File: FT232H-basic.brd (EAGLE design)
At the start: 45.7 x 20.3 mm, 29 parts, among them IC1 FT232H

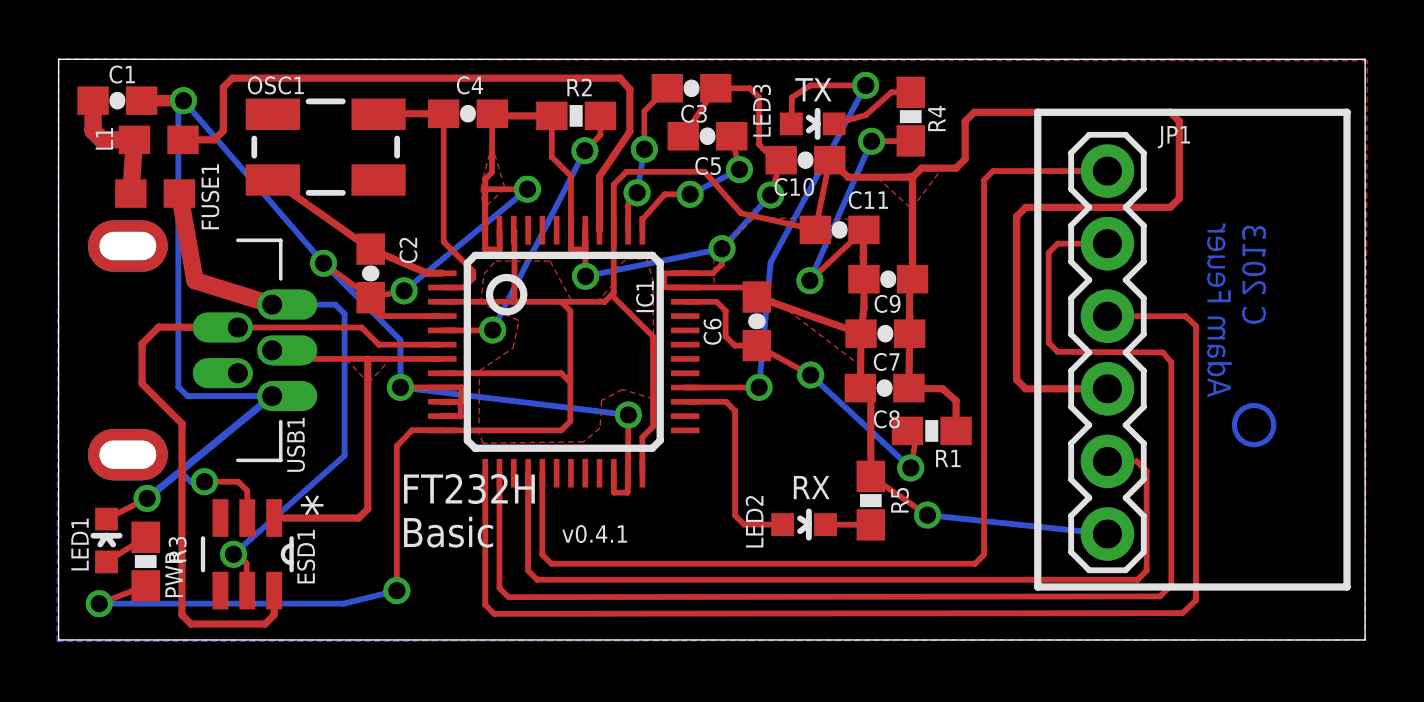
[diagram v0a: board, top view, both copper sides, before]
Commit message: replaced decoupling capacitors close to chip; rerouted board
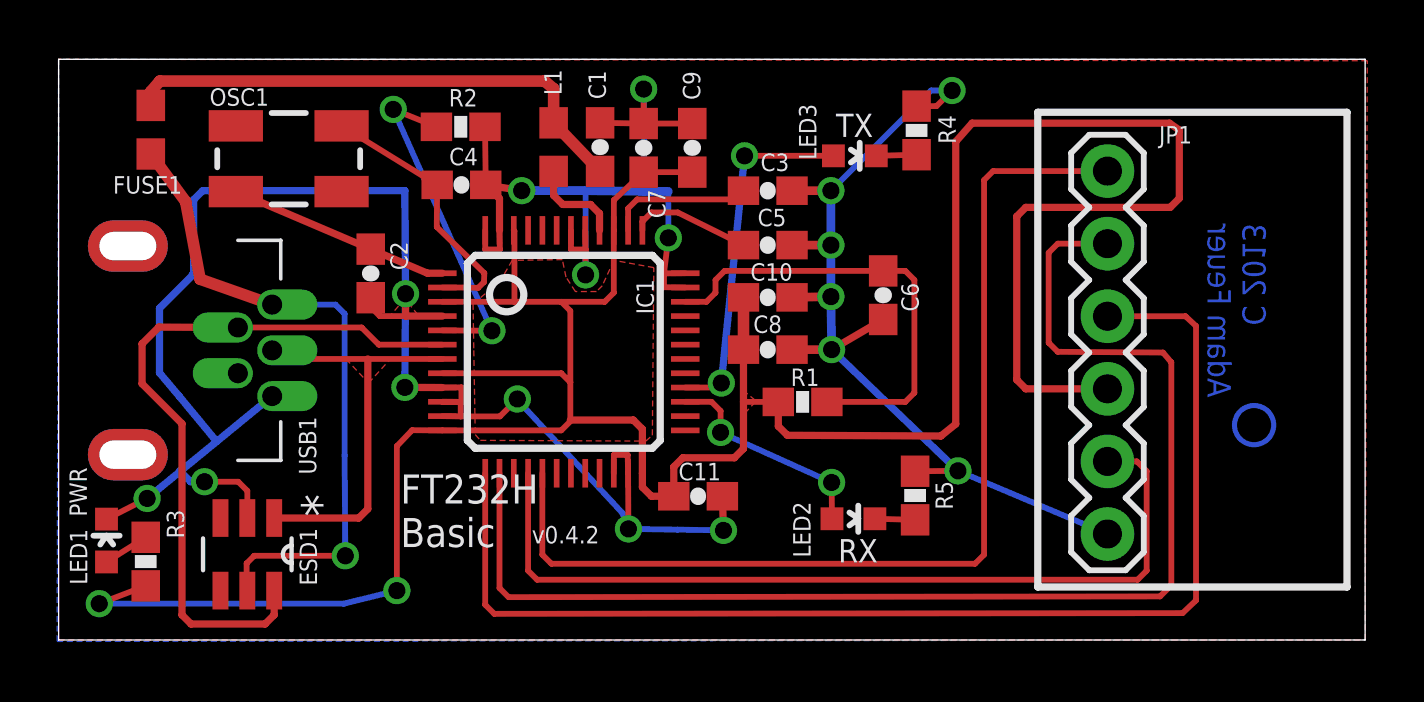
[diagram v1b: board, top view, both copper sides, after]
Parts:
- moved C1 17.0 mm to (25.3, 21.1), turned to 90 degrees
- moved L1 13.8 mm to (23.7, 21.1), turned to 270 degrees
- moved C7 10.7 mm to (26.8, 21.0), turned to 90 degrees
- moved C11 10.6 mm to (28.7, 8.84)
- moved C9 8.26 mm to (28.5, 21.0), turned to 90 degrees
- moved C10 4.98 mm to (31.2, 15.8), turned to 0 degrees
- moved R1 4.63 mm to (32.4, 12.1), turned to 180 degrees
- moved C6 4.51 mm to (35.2, 15.9), turned to 270 degrees
- moved C3 4.47 mm to (31.2, 19.5)
- moved C5 4.35 mm to (31.2, 17.6), turned to 0 degrees
- moved C8 4.31 mm to (31.2, 14.0), turned to 0 degrees
- moved R2 4.06 mm to (20.4, 21.8), turned to 180 degrees
- moved C4 2.50 mm to (20.4, 19.7)
- moved FUSE1 2.24 mm to (9.58, 21.7), turned to 90 degrees
- moved LED3 1.85 mm to (34.2, 20.8)
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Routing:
- net VREGIN: track 22.9 -> 3.30 mm
- net N$6: track 4.52 -> 18.4 mm
- net GND: track 138.7 -> 125.7 mm, vias 14 -> 17
- net TXLED: track 17.6 -> 12.4 mm
- net N$3: track 12.0 -> 16.0 mm, vias 2 -> 0
- net VUSB: track 20.3 -> 23.2 mm
- net N$10: track 3.02 -> 1.41 mm
- net N$4: track 10.3 -> 11.8 mm
- net N$1: track 5.58 -> 4.25 mm, vias 2 -> 0
- net POWER: track 105.4 -> 106.6 mm
- net OSC1: track 6.87 -> 7.81 mm
- net N$2: track 5.43 -> 5.06 mm, vias 2 -> 0
- net RXLED: track 7.33 -> 7.65 mm, vias 0 -> 2
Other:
- board text added: "v0.4.2"
- board text removed: "v0.4.1"

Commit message: moved OSC1 traces so they are not serpentine
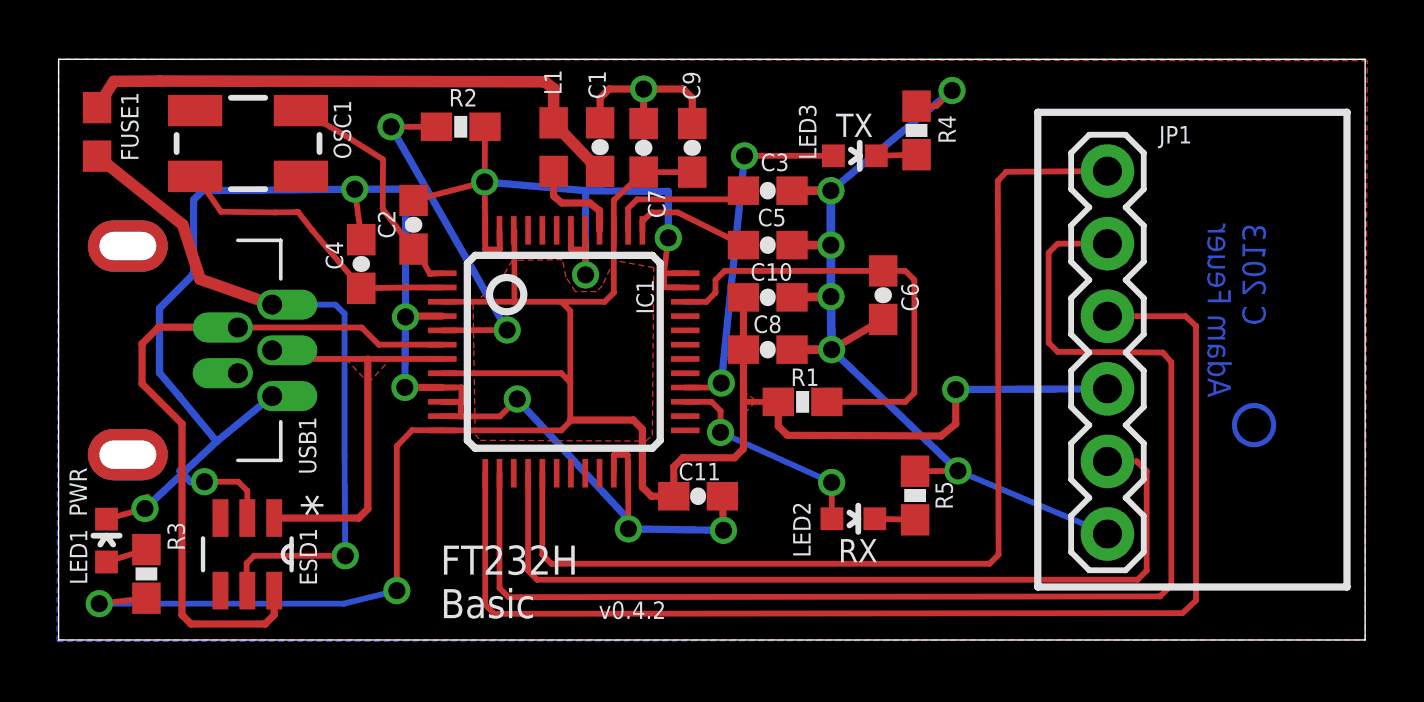
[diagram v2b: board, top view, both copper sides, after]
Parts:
- removed FRAME1: FRAME-LETTER, SparkFun-Aesthetics:CREATIVE_COMMONS
- moved U$1 19.9 mm to (38.1, 17.1)
- moved CC-BY-SA-LOGO 11.8 mm to (41.5, 4.37)
- moved C4 4.47 mm to (16.9, 17.0), turned to 90 degrees
- moved C2 2.27 mm to (18.8, 18.3), turned to 90 degrees
- moved FUSE1 1.88 mm to (7.70, 21.6)
- moved OSC1 1.52 mm to (13.0, 21.2), turned to 180 degrees
- moved R3 0.43 mm to (9.42, 6.12)
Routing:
- net POWER: track 106.6 -> 77.6 mm, vias 2 -> 3
- net GND: track 125.7 -> 128.5 mm, vias 17 -> 18
- net N$6: track 18.4 -> 20.1 mm
- net VUSB: track 23.2 -> 24.2 mm
- net N$7: track 9.58 -> 10.5 mm
- net OSC1: track 7.81 -> 8.34 mm
- removed copper zone on layer 1, net GND
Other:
- board text added: "3.3V"
- board text removed: "5V"

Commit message: moved VUSB trace so it doesn't cross under USB DP and DM - so there is only ground plane under the high speed traces
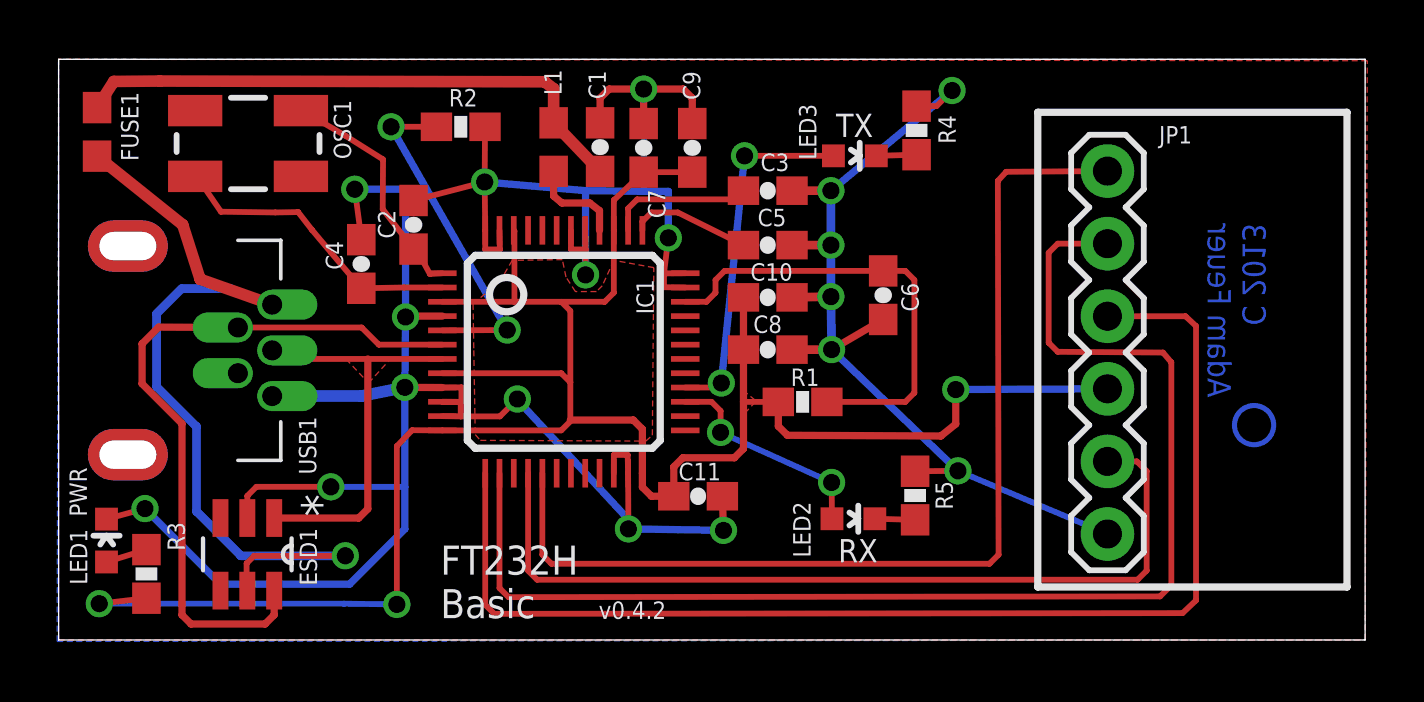
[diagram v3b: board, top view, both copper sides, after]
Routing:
- net VUSB: track 24.2 -> 30.9 mm
- net GND: track 128.5 -> 130.1 mm
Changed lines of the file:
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@@
 <contactref element="JP1" pad="6"/>
 <contactref element="C1" pad="2"/>
-<wire x1="9.4606" y1="8.802" x2="9.3726" y2="8.4074" width="0.254" layer="1"/>
 <via x="9.3726" y="8.4074" extent="1-16" drill="0.6"/>
-<wire x1="9.3726" y1="8.4074" x2="11.88134375" y2="10.75440625" width="0.254" layer="16"/>
-<wire x1="11.88134375" y1="10.75440625" x2="13.8238" y2="12.3446" width="0.254" layer="16"/>
-<wire x1="12.954" y1="8.0772" x2="12.954" y2="9.0297" width="0.2032" layer="1"/>
-<wire x1="12.954" y1="9.0297" x2="12.6365" y2="9.3472" width="0.2032" layer="1"/>
-<wire x1="12.6365" y1="9.3472" x2="11.4554" y2="9.3472" width="0.2032" layer="1"/>
-<via x="11.4554" y="9.3472" extent="1-16" drill="0.6"/>
-<wire x1="11.4554" y1="9.3472" x2="10.9727625" y2="9.3472" width="0.254" layer="16"/>
-<wire x1="10.9727625" y1="9.3472" x2="10.587325" y2="9.7326375" width="0.254" layer="16"/>
 <wire x1="24.2784" y1="17.4752" x2="24.2784" y2="18.1438" width="0.2032" layer="1"/>
 <wire x1="19.7784" y1="11.6438" x2="20.4216" y2="11.6332" width="0.2032" layer="1"/>
@@
 <wire x1="24.7904" y1="19.5326" x2="21.2598" y2="19.8374" width="0.254" layer="16"/>
 <wire x1="18.4912" y1="19.5834" x2="16.7132" y2="19.5834" width="0.254" layer="16"/>
-<wire x1="16.7132" y1="19.5834" x2="11.3919" y2="19.5326" width="0.254" layer="16"/>
-<wire x1="11.3919" y1="19.5326" x2="11.0744" y2="19.2151" width="0.254" layer="16"/>
-<wire x1="11.0744" y1="19.2151" x2="11.0744" y2="16.5862" width="0.254" layer="16"/>
-<wire x1="11.0744" y1="16.5862" x2="11.049" y2="16.5862" width="0.3048" layer="16"/>
-<wire x1="11.049" y1="16.5862" x2="9.8806" y2="15.4178" width="0.254" layer="16"/>
-<wire x1="9.8806" y1="15.4178" x2="9.8806" y2="13.1572" width="0.254" layer="16"/>
-<wire x1="9.8806" y1="13.1572" x2="10.5664" y2="12.3444" width="0.254" layer="16"/>
 <wire x1="32.0158" y1="17.6276" x2="33.3756" y2="17.6276" width="0.3048" layer="1"/>
 <via x="33.3756" y="17.6276" extent="1-16" drill="0.6"/>
@@
 <wire x1="37.0704" y1="22.4908" x2="37.6174" y2="23.0378" width="0.2032" layer="1"/>
 <via x="37.6174" y="23.0378" extent="1-16" drill="0.6"/>
-<wire x1="10.5664" y1="12.3444" x2="11.88134375" y2="10.75440625" width="0.254" layer="16"/>
 <wire x1="33.3756" y1="19.5326" x2="37.6174" y2="23.0378" width="0.254" layer="16"/>
 <wire x1="21.2716" y1="21.7678" x2="21.2598" y2="19.8374" width="0.2032" layer="1"/>
@@
 <wire x1="28.5242" y1="22.7711" x2="28.2067" y2="23.0886" width="0.254" layer="1"/>
 <wire x1="28.2067" y1="23.0886" x2="26.8224" y2="23.0886" width="0.254" layer="1"/>
+<wire x1="9.3726" y1="8.4074" x2="12.0142" y2="5.7658" width="0.254" layer="16"/>
+<wire x1="12.0142" y1="5.7658" x2="16.5354" y2="5.7658" width="0.254" layer="16"/>
+<wire x1="16.5354" y1="5.7658" x2="18.4658" y2="7.6962" width="0.254" layer="16"/>
+<wire x1="18.4658" y1="7.6962" x2="18.4658" y2="9.1694" width="0.254" layer="16"/>
+<wire x1="18.4658" y1="9.1694" x2="18.4658" y2="12.6492" width="0.254" layer="16"/>
+<wire x1="12.954" y1="8.0772" x2="12.954" y2="8.8519" width="0.2032" layer="1"/>
+<wire x1="12.954" y1="8.8519" x2="13.2715" y2="9.1694" width="0.2032" layer="1"/>
+<wire x1="13.2715" y1="9.1694" x2="15.875" y2="9.1694" width="0.2032" layer="1"/>
+<via x="15.875" y="9.1694" extent="1-16" drill="0.6"/>
+<wire x1="15.875" y1="9.1694" x2="18.4658" y2="9.1694" width="0.2032" layer="16"/>
+<wire x1="13.8238" y1="12.3446" x2="16.942" y2="12.3446" width="0.4064" layer="16"/>
+<wire x1="16.942" y1="12.3446" x2="18.4658" y2="12.6492" width="0.4064" layer="16"/>
 </signal>
 <signal name="OSC1">
@@
 <wire x1="12.954" y1="5.5372" x2="12.9286" y2="5.5626" width="0.254" layer="1"/>
 <via x="16.383" y="6.7564" extent="1-16" drill="0.6"/>
-<wire x1="16.3576" y1="15.2271" x2="16.0401" y2="15.5446" width="0.2032" layer="16"/>
-<wire x1="16.0401" y1="15.5446" x2="13.8238" y2="15.5446" width="0.2032" layer="16"/>
-<wire x1="16.3576" y1="15.2271" x2="16.3576" y2="10.2616" width="0.2032" layer="16"/>
-<wire x1="16.3576" y1="10.2616" x2="16.383" y2="6.7564" width="0.2032" layer="16"/>
 <wire x1="12.9286" y1="5.5626" x2="12.9286" y2="6.4897" width="0.2032" layer="1"/>
 <wire x1="12.9286" y1="6.4897" x2="13.1953" y2="6.7564" width="0.2032" layer="1"/>
@@
 <wire x1="11.303" y1="16.4338" x2="10.6934" y2="18.3388" width="0.4064" layer="1"/>
 <wire x1="10.6934" y1="18.3388" x2="7.6962" y2="20.74" width="0.4064" layer="1"/>
+<wire x1="13.8238" y1="15.5446" x2="12.3698" y2="16.1036" width="0.3048" layer="16"/>
+<wire x1="12.3698" y1="16.1036" x2="10.6555" y2="16.1036" width="0.3048" layer="16"/>
+<wire x1="10.6555" y1="16.1036" x2="9.779" y2="15.2271" width="0.3048" layer="16"/>
+<wire x1="9.779" y1="15.2271" x2="9.779" y2="12.6746" width="0.3048" layer="16"/>
+<wire x1="9.779" y1="12.6746" x2="11.176" y2="11.2776" width="0.3048" layer="16"/>
+<wire x1="11.176" y1="11.2776" x2="11.176" y2="8.3058" width="0.3048" layer="16"/>
+<wire x1="11.176" y1="8.3058" x2="12.7254" y2="6.7564" width="0.3048" layer="16"/>
+<wire x1="12.7254" y1="6.7564" x2="16.383" y2="6.7564" width="0.3048" layer="16"/>
 </signal>
 <signal name="DP">
@@
 <via x="7.7724" y="5.08" extent="1-16" drill="0.6"/>
 <wire x1="7.7724" y1="5.08" x2="16.3322" y2="5.08" width="0.2032" layer="16"/>
-<wire x1="16.3322" y1="5.08" x2="18.1864" y2="5.5372" width="0.2032" layer="16"/>
-<via x="18.1864" y="5.5372" extent="1-16" drill="0.6"/>
-<wire x1="18.1864" y1="5.5372" x2="18.1864" y2="10.5918" width="0.2032" layer="1"/>
+<wire x1="16.3322" y1="5.08" x2="18.1864" y2="5.0546" width="0.2032" layer="16"/>
+<via x="18.1864" y="5.0546" extent="1-16" drill="0.6"/>
+<wire x1="18.1864" y1="5.0546" x2="18.1864" y2="10.5918" width="0.2032" layer="1"/>
 <wire x1="18.1864" y1="10.5918" x2="18.7198" y2="11.1506" width="0.2032" layer="1"/>
 <wire x1="18.7198" y1="11.1506" x2="19.7784" y2="11.1438" width="0.2032" layer="1"/>

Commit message: minor updates to board legend; added BOM files and board PDF
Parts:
- added FRAME1: FRAME-LETTER, SparkFun-Aesthetics:CREATIVE_COMMONS
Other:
- board text added: "v0.4.3"
- board text removed: "v0.4.2"
